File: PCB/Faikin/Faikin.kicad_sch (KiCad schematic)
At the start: 49 parts, among them J1 1x5, J2 TC2030-USB-NL, J3 Reset, Q1 BSS138PS, U1 TPS562246, U4 ESP32-S3-MINI-1

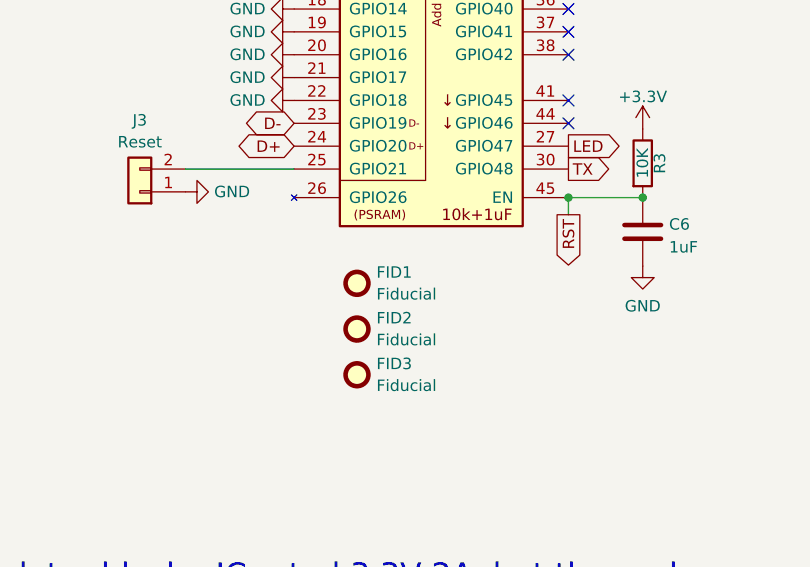
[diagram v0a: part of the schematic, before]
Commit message: Thicker top
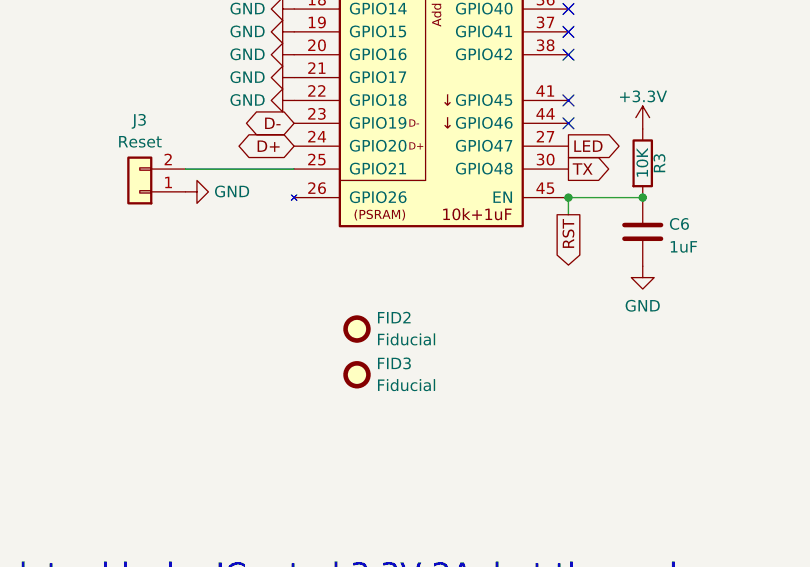
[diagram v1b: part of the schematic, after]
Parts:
- removed FID1: Fiducial, Fiducial:Fiducial_1mm_Mask2mm, symbol Mechanical:Fiducial
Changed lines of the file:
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@@
-	(symbol
-		(lib_id "Mechanical:Fiducial")
-		(at 90.805 118.745 0)
-		(unit 1)
-		(exclude_from_sim no)
-		(in_bom no)
-		(on_board yes)
-		(dnp no)
-		(fields_autoplaced yes)
-		(property "Reference" "FID1"
-			(at 92.964 117.5328 0)
-			(effects
-				(font
-					(size 1.27 1.27)
-				)
-				(justify left)
-			)
-		)
-		(property "Value" "Fiducial"
-			(at 92.964 119.9571 0)
-			(effects
-				(font
-					(size 1.27 1.27)
-				)
-				(justify left)
-			)
-		)
-		(property "Footprint" "Fiducial:Fiducial_1mm_Mask2mm"
-			(at 90.805 118.745 0)
-			(effects
-				(font
-					(size 1.27 1.27)
-				)
-				(hide yes)
-			)
-		)
-		(property "Datasheet" "~"
-			(at 90.805 118.745 0)
-			(effects
-				(font
-					(size 1.27 1.27)
-				)
-				(hide yes)
-			)
-		)
-		(property "Description" "Fiducial Marker"
-			(at 90.805 118.745 0)
-			(effects
-				(font
-					(size 1.27 1.27)
-				)
-				(hide yes)
-			)
-		)
-		(instances
-			(project ""
-				(path "/46c350bb-7de4-4e81-aafd-4af55e37aab0"
-					(reference "FID1")
-					(unit 1)
-				)
-			)
-		)
-	)
 	(symbol
 		(lib_id "Mechanical:Fiducial")

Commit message: Library update
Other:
- title: Daikin ESP32-PICO-MINI module -> Faikin
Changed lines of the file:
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@@
 	(paper "A4")
 	(title_block
-		(title "Daikin ESP32-PICO-MINI module")
+		(title "Faikin")
 		(rev "1")
 		(comment 1 "@TheRealRevK")
@@
 		(on_board yes)
 		(dnp no)
-		(fields_autoplaced yes)
 		(property "Reference" "TP2"
-			(at 171.323 141.2705 90)
+			(at 174.752 140.8317 90)
 			(effects
 				(font
@@
 		)
 		(property "Value" "TestPoint"
-			(at 171.323 143.6948 90)
+			(at 174.752 143.256 90)
 			(effects
 				(font
@@
 		(on_board yes)
 		(dnp no)
-		(fields_autoplaced yes)
 		(property "Reference" "TP5"
-			(at 209.423 141.2705 90)
+			(at 212.852 140.8317 90)
 			(effects
 				(font
@@
 		)
 		(property "Value" "TestPoint"
-			(at 209.423 143.6948 90)
+			(at 212.852 143.256 90)
 			(effects
 				(font
@@
 		(on_board yes)
 		(dnp no)
-		(fields_autoplaced yes)
 		(property "Reference" "TP4"
-			(at 196.723 141.2705 90)
+			(at 200.152 140.8317 90)
 			(effects
 				(font
@@
 		)
 		(property "Value" "TestPoint"
-			(at 196.723 143.6948 90)
+			(at 200.152 143.256 90)
 			(effects
 				(font
@@
 		(on_board yes)
 		(dnp no)
-		(fields_autoplaced yes)
 		(property "Reference" "TP8"
-			(at 247.523 141.2705 90)
+			(at 250.952 140.8317 90)
 			(effects
 				(font
@@
 		)
 		(property "Value" "TestPoint"
-			(at 247.523 143.6948 90)
+			(at 250.952 143.256 90)
 			(effects
 				(font
@@
 		(on_board yes)
 		(dnp no)
-		(fields_autoplaced yes)
 		(property "Reference" "TP6"
-			(at 222.123 141.2705 90)
+			(at 225.552 140.8317 90)
 			(effects
 				(font
@@
 		)
 		(property "Value" "TestPoint"
-			(at 222.123 143.6948 90)
+			(at 225.552 143.256 90)
 			(effects
 				(font
@@
 		(dnp no)
 		(property "Reference" "R3"
-			(at 124.46 105.41 90)
+			(at 125.222 105.41 90)
 			(effects
 				(font
@@
 		(on_board yes)
 		(dnp no)
-		(fields_autoplaced yes)
 		(property "Reference" "TP10"
-			(at 145.923 141.2705 90)
+			(at 149.352 140.8317 90)
 			(effects
 				(font
@@
 		)
 		(property "Value" "TestPoint"
-			(at 145.923 143.6948 90)
+			(at 149.352 143.256 90)
 			(effects
 				(font
@@
 		(on_board yes)
 		(dnp no)
-		(fields_autoplaced yes)
 		(property "Reference" "TP3"
-			(at 184.023 141.2705 90)
+			(at 187.452 140.8317 90)
 			(effects
 				(font
@@
 		)
 		(property "Value" "TestPoint"
-			(at 184.023 143.6948 90)
+			(at 187.452 143.256 90)
 			(effects
 				(font
@@
 		(on_board yes)
 		(dnp no)
-		(fields_autoplaced yes)
 		(property "Reference" "TP7"
-			(at 234.823 141.2705 90)
+			(at 238.252 140.8317 90)
 			(effects
 				(font
@@
 		)
 		(property "Value" "TestPoint"
-			(at 234.823 143.6948 90)
+			(at 238.252 143.256 90)
 			(effects
 				(font
@@
 		(on_board yes)
 		(dnp no)
-		(fields_autoplaced yes)
 		(property "Reference" "TP9"
-			(at 158.623 141.2705 90)
+			(at 162.052 140.8317 90)
 			(effects
 				(font
@@
 		)
 		(property "Value" "TestPoint"
-			(at 158.623 143.6948 90)
+			(at 162.052 143.256 90)
 			(effects
 				(font

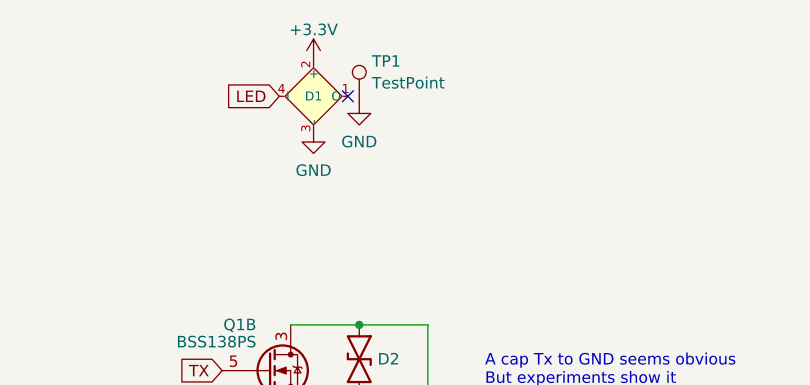
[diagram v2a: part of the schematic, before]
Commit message: TC2030 on top
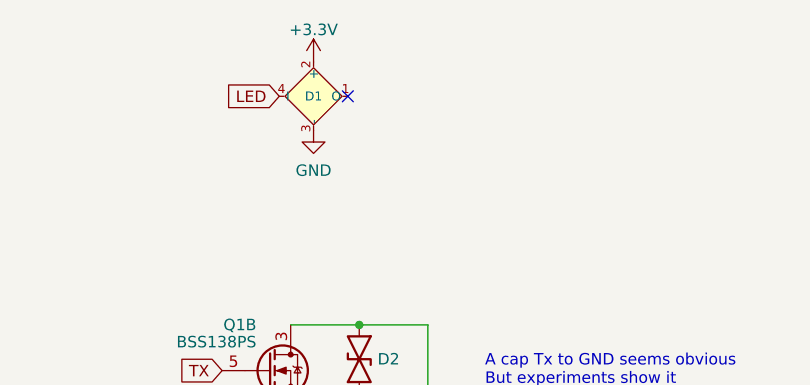
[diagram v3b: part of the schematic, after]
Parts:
- removed TP1: TestPoint, RevK:1x2-Hole, symbol Connector:TestPoint
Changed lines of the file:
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@@
-	)
-	(symbol
-		(lib_id "Connector:TestPoint")
-		(at 167.005 46.99 0)
-		(unit 1)
-		(exclude_from_sim no)
-		(in_bom no)
-		(on_board yes)
-		(dnp no)
-		(fields_autoplaced yes)
-		(property "Reference" "TP1"
-			(at 168.402 42.4758 0)
-			(effects
-				(font
-					(size 1.27 1.27)
-				)
-				(justify left)
-			)
-		)
-		(property "Value" "TestPoint"
-			(at 168.402 44.9001 0)
-			(effects
-				(font
-					(size 1.27 1.27)
-				)
-				(justify left)
-			)
-		)
-		(property "Footprint" "RevK:1x2-Hole"
-			(at 172.085 46.99 0)
-			(effects
-				(font
-					(size 1.27 1.27)
-				)
-				(hide yes)
-			)
-		)
-		(property "Datasheet" "~"
-			(at 172.085 46.99 0)
-			(effects
-				(font
-					(size 1.27 1.27)
-				)
-				(hide yes)
-			)
-		)
-		(property "Description" "test point"
-			(at 167.005 46.99 0)
-			(effects
-				(font
-					(size 1.27 1.27)
-				)
-				(hide yes)
-			)
-		)
-		(pin "1"
-		)
-		(instances
-			(project ""
-				(path "/46c350bb-7de4-4e81-aafd-4af55e37aab0"
-					(reference "TP1")
-					(unit 1)
-				)
-			)
-		)
 	)
 	(symbol
@@
 					(unit 1)
 				)
-			)
-		)
-	)
-	(symbol
-		(lib_id "power:GND")
-		(at 167.005 46.99 0)
-		(unit 1)
-		(exclude_from_sim no)
-		(in_bom yes)
-		(on_board yes)
-		(dnp no)
-		(fields_autoplaced yes)
-		(property "Reference" "#PWR027"
-			(at 167.005 53.34 0)
-			(effects
-				(font
-					(size 1.27 1.27)
-				)
-				(hide yes)
-			)
-		)
-		(property "Value" "GND"
-			(at 167.005 51.4334 0)
-			(effects
-				(font
-					(size 1.27 1.27)
-				)
-			)
-		)
-		(property "Footprint" ""
-			(at 167.005 46.99 0)
-			(effects
-				(font
-					(size 1.27 1.27)
-				)
-				(hide yes)
-			)
-		)
-		(property "Datasheet" ""
-			(at 167.005 46.99 0)
-			(effects
-				(font
-					(size 1.27 1.27)
-				)
-				(hide yes)
-			)
-		)
-		(property "Description" "Power symbol creates a global label with name \"GND\" , ground"
-			(at 167.005 46.99 0)
-			(effects
-				(font
-					(size 1.27 1.27)
-				)
-				(hide yes)
-			)
-		)
-		(pin "1"
-		)
-		(instances
-			(project "Faikin"
-				(path "/46c350bb-7de4-4e81-aafd-4af55e37aab0"
-					(reference "#PWR027")
-					(unit 1)
-				)
